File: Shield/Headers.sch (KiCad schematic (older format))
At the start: 18 parts, among them J1 EXPANSION, J12 CONN_6, J23 POWER IN, J24 GND V_IN, J28 Probe, J8 Y MOT/STOP, J9 X MOT/STOP

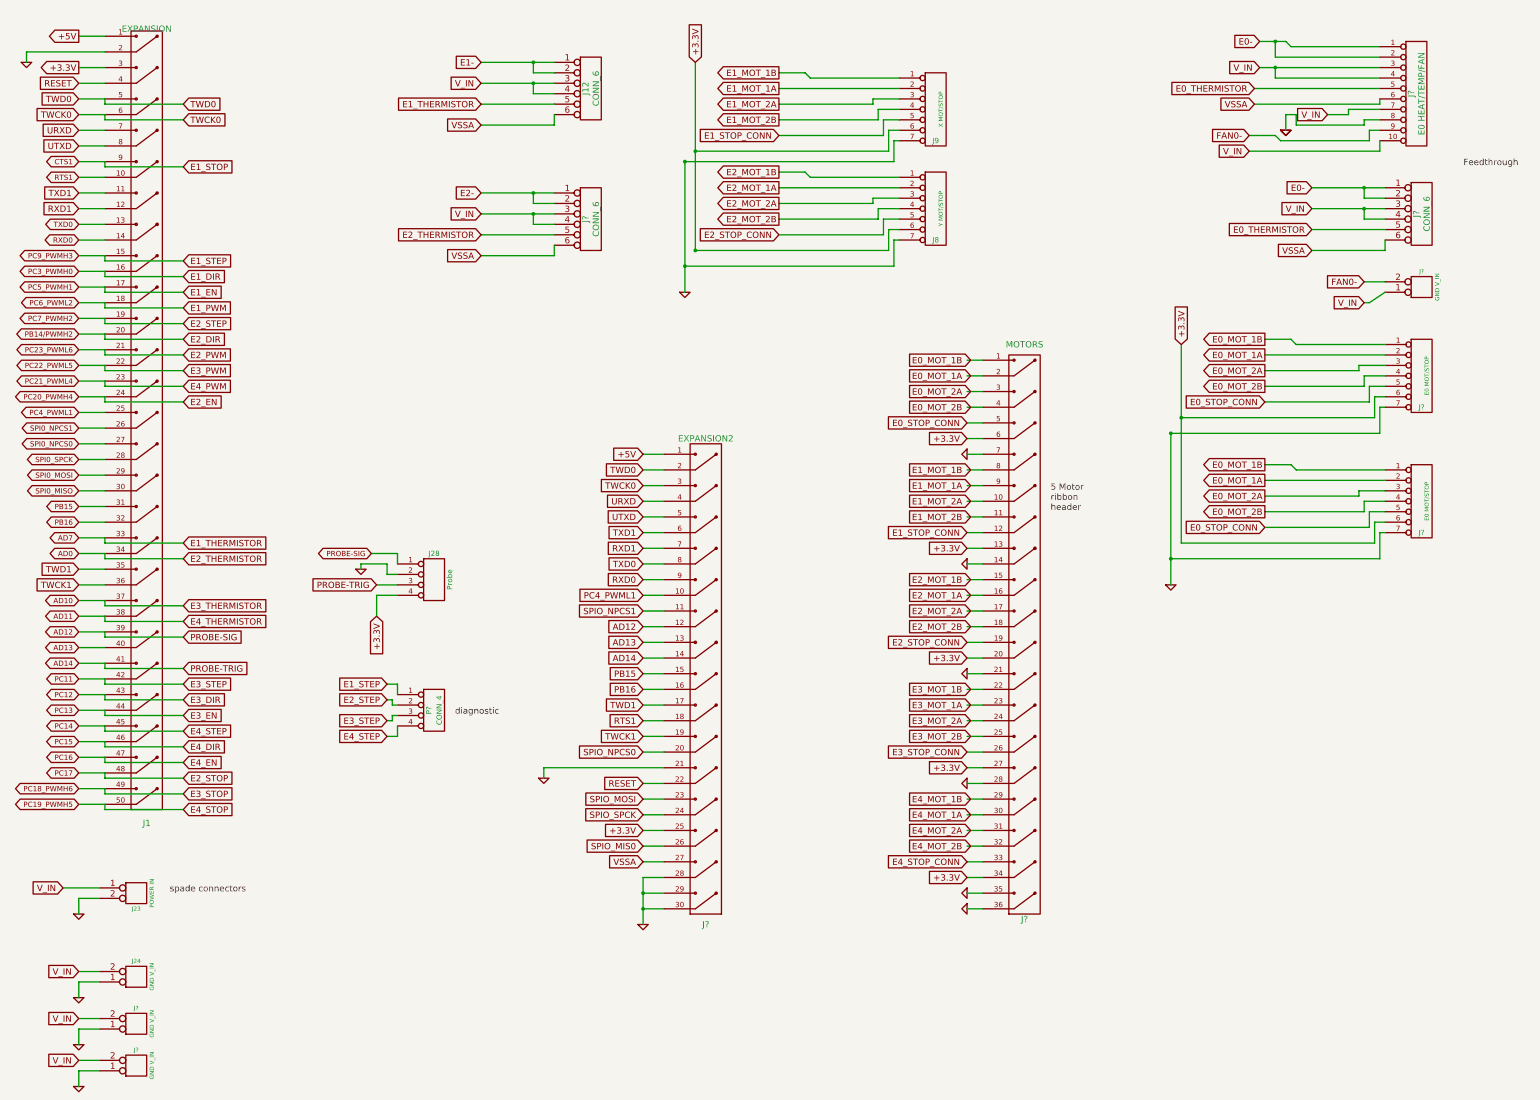
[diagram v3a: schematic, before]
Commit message: Inputs and outputs tidied to keep DRC a bit happier...
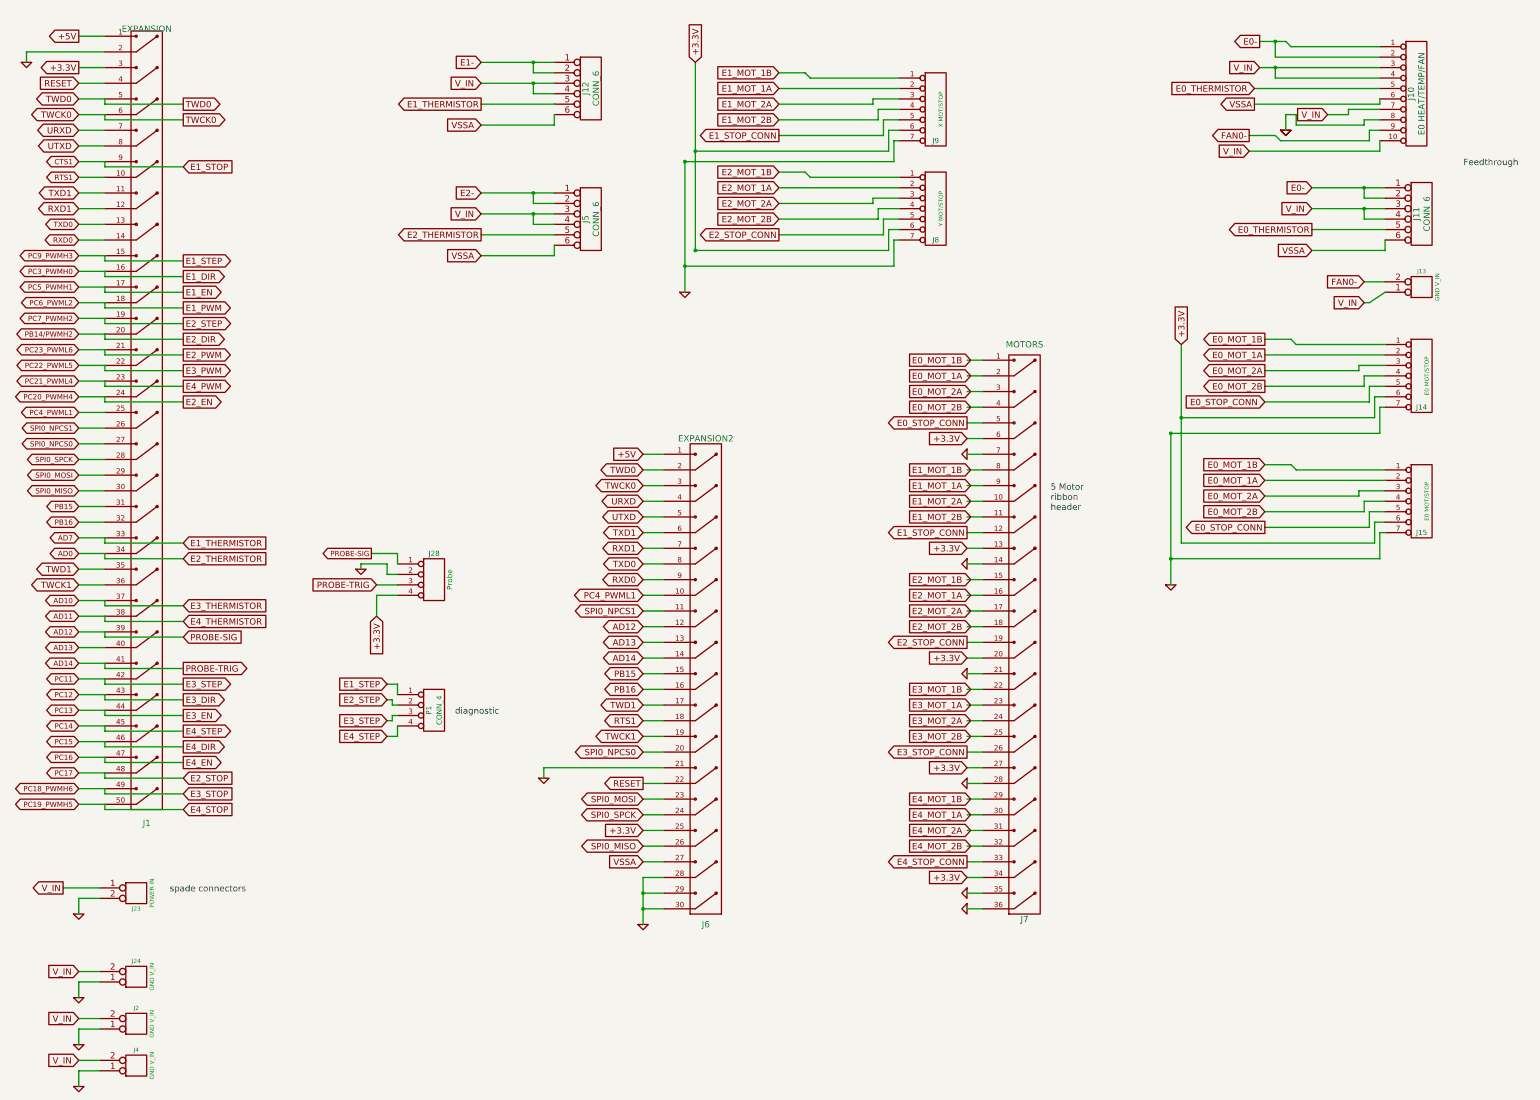
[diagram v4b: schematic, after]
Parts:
- gave numbers to parts that had none: 11
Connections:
- net labels removed: SPIO_MIS0, SPIO_MOSI, SPIO_NPCS0, SPIO_NPCS1, SPIO_SPCK
- wire segments 357 -> 343

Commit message: Header labels corrected.
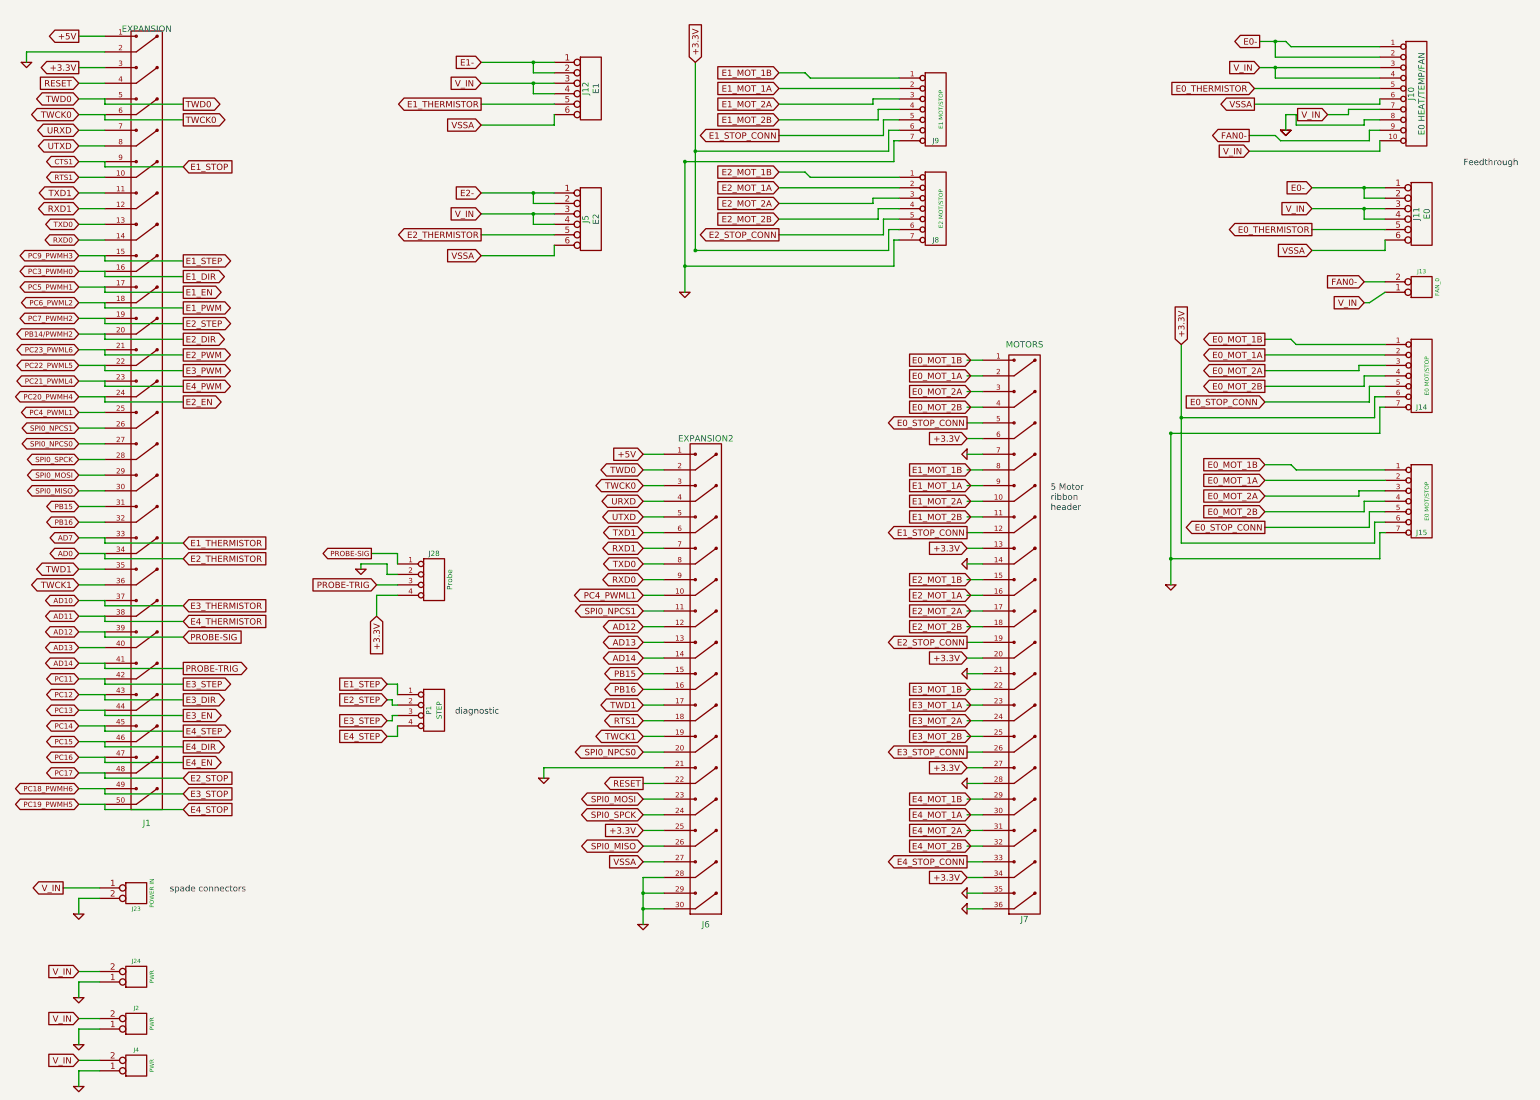
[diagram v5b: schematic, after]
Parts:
- J11: value CONN_6 -> E0
- J12: value CONN_6 -> E1
- J13: value GND V_IN -> FAN_0
- J2, J24, J4: value GND V_IN -> PWR
- J5: value CONN_6 -> E2
- J8: value Y MOT/STOP -> E2 MOT/STOP
- J9: value X MOT/STOP -> E1 MOT/STOP
- P1: value CONN_4 -> STEP
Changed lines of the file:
@@
-EESchema Schematic File Version 2  date Fri 07 Nov 2014 11:38:16 GMT
+EESchema Schematic File Version 2  date Fri 07 Nov 2014 14:33:05 GMT
 LIBS:power
 LIBS:device
@@
 P 5000 7150
 F 0 "P1" V 4950 7150 50  0000 C CNN
-F 1 "CONN_4" V 5050 7150 50  0000 C CNN
+F 1 "STEP" V 5050 7150 50  0000 C CNN
 	1    5000 7150
 	1    0    0    -1
@@
 P 14450 3050
 F 0 "J13" H 14450 2950 40  0000 C CNN
-F 1 "GND  V_IN" V 14600 3100 40  0000 C CNN
+F 1 "FAN_0" V 14600 3100 40  0000 C CNN
 	1    14450 3050
 	1    0    0    1
@@
 P 14450 2400
 F 0 "J11" V 14400 2400 60  0000 C CNN
-F 1 "CONN_6" V 14500 2400 60  0000 C CNN
+F 1 "E0" V 14500 2400 60  0000 C CNN
 	1    14450 2400
 	1    0    0    -1
@@
 P 2150 10500
 F 0 "J4" H 2150 10400 40  0000 C CNN
-F 1 "GND  V_IN" V 2300 10550 40  0000 C CNN
+F 1 "PWR" V 2300 10550 40  0000 C CNN
 	1    2150 10500
 	1    0    0    1
@@
 P 2150 10100
 F 0 "J2" H 2150 10000 40  0000 C CNN
-F 1 "GND  V_IN" V 2300 10150 40  0000 C CNN
+F 1 "PWR" V 2300 10150 40  0000 C CNN
 	1    2150 10100
 	1    0    0    1
@@
 P 6500 2450
 F 0 "J5" V 6450 2450 60  0000 C CNN
-F 1 "CONN_6" V 6550 2450 60  0000 C CNN
+F 1 "E2" V 6550 2450 60  0000 C CNN
 	1    6500 2450
 	1    0    0    -1
@@
 P 6500 1200
 F 0 "J12" V 6450 1200 60  0000 C CNN
-F 1 "CONN_6" V 6550 1200 60  0000 C CNN
+F 1 "E1" V 6550 1200 60  0000 C CNN
 	1    6500 1200
 	1    0    0    -1
@@
 P 2150 9650
 F 0 "J24" H 2150 9550 40  0000 C CNN
-F 1 "GND  V_IN" V 2300 9700 40  0000 C CNN
+F 1 "PWR" V 2300 9700 40  0000 C CNN
 	1    2150 9650
 	1    0    0    1
@@
 P 9800 1400
 F 0 "J9" H 9800 1100 50  0000 C CNN
-F 1 "X MOT/STOP" V 9850 1400 40  0000 C CNN
+F 1 "E1 MOT/STOP" V 9850 1400 40  0000 C CNN
 	1    9800 1400
 	1    0    0    -1
@@
 P 9800 2350
 F 0 "J8" H 9800 2050 50  0000 C CNN
-F 1 "Y MOT/STOP" V 9850 2350 40  0000 C CNN
+F 1 "E2 MOT/STOP" V 9850 2350 40  0000 C CNN
 	1    9800 2350
 	1    0    0    -1

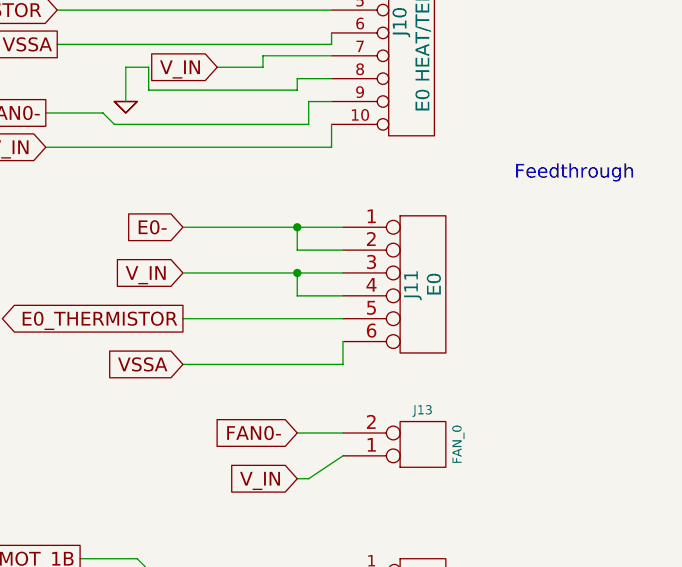
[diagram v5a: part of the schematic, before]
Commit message: Started PCB layout for Shield.
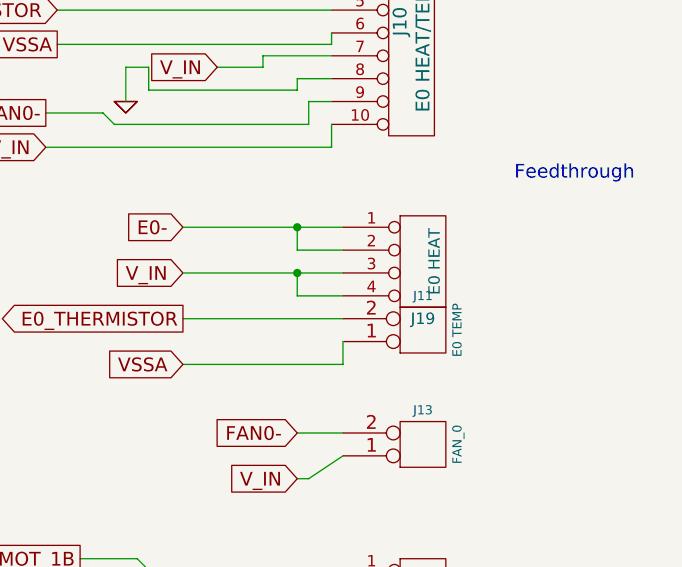
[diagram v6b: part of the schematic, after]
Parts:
- removed J11: E0, symbol CONN_6
- added J11: E0 TEMP, symbol CONN2
- added J19: E0 HEAT, symbol CONN4
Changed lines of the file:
@@
-EESchema Schematic File Version 2  date Fri 07 Nov 2014 14:33:05 GMT
+EESchema Schematic File Version 2  date Thu 13 Nov 2014 23:27:25 GMT
 LIBS:power
 LIBS:device
@@
 Sheet 3 4
 Title "Duet"
-Date "7 nov 2014"
+Date "13 nov 2014"
 Rev "0.7"
 Comp "Think3DPrint3D, RepRapPro"
@@
 Comment4 ""
 $EndDescr
+$Comp
+L CONN4 J19
+U 1 1 5465390C
+P 14450 2300
+F 0 "J19" H 14450 2050 50  0000 C CNN
+F 1 "E0 HEAT" V 14500 2300 50  0000 C CNN
+	1    14450 2300
+	1    0    0    -1
+$EndComp
+$Comp
+L CONN2 J11
+U 1 1 5464EB0A
+P 14450 2550
+F 0 "J11" H 14450 2450 40  0000 C CNN
+F 1 "E0 TEMP" V 14600 2600 40  0000 C CNN
+	1    14450 2550
+	1    0    0    1
+$EndComp
 Text GLabel 7000 6650 0    60   BiDi ~ 0
 AD14
@@
 Text GLabel 13900 3050 0    60   Input ~ 0
 FAN0-
-$Comp
-L CONN_6 J11
-U 1 1 545B8869
-P 14450 2400
-F 0 "J11" V 14400 2400 60  0000 C CNN
-F 1 "E0" V 14500 2400 60  0000 C CNN
-	1    14450 2400
-	1    0    0    -1
-$EndComp
 Text GLabel 13400 2150 0    60   Input ~ 0
 E0-

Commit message: Minor tidying...
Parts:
- removed J10: E0 HEAT/TEMP/FAN, symbol CONN_10
- added J10: CONN2, symbol CONN2
- added K1: CONN_3, symbol CONN_3
- added P2: CONN_6, symbol CONN_6
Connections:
- wire segments 343 -> 347

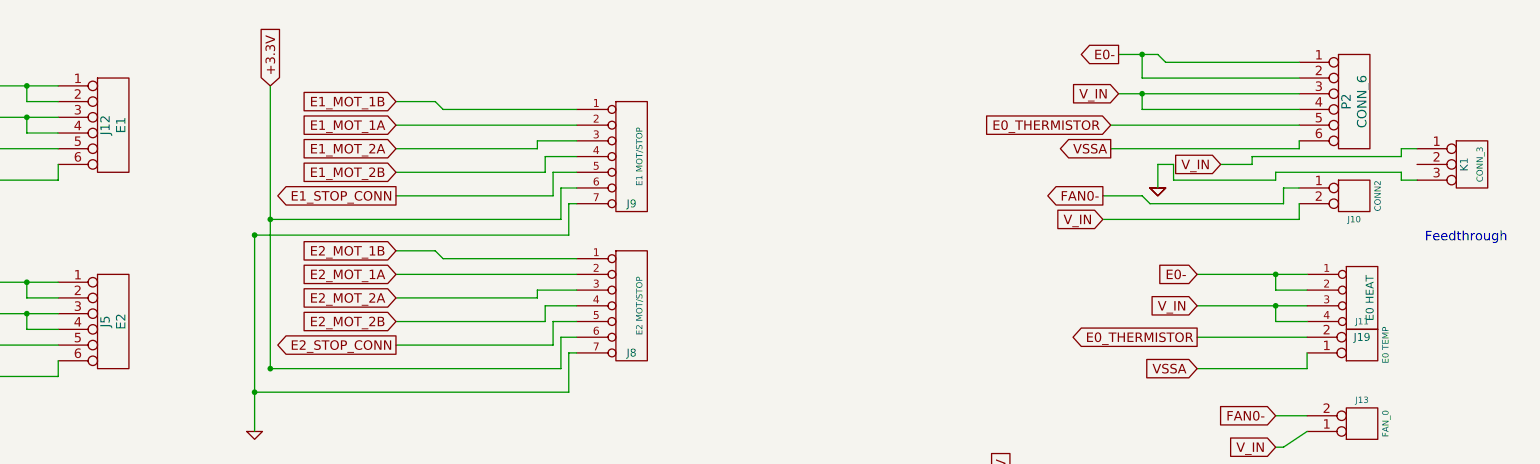
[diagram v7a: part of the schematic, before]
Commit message: Some pin headers provisionally positioned.
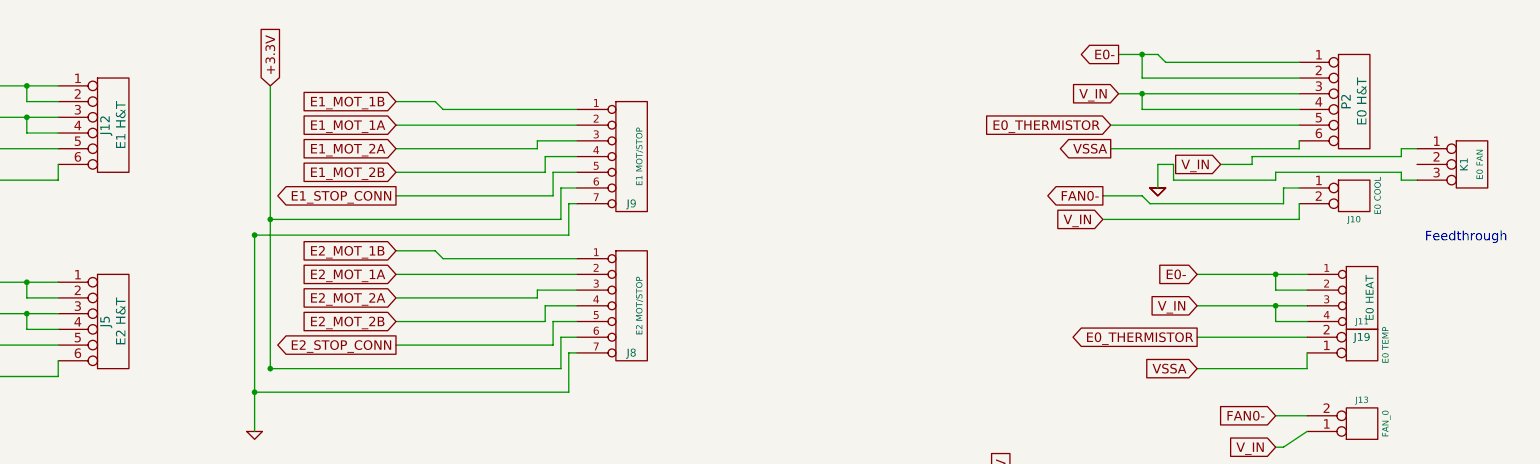
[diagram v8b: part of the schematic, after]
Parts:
- J10: value CONN2 -> E0 COOL
- J12: value E1 -> E1 H&T
- J5: value E2 -> E2 H&T
- K1: value CONN_3 -> E0 FAN
- P2: value CONN_6 -> E0 H&T
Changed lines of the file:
@@
-EESchema Schematic File Version 2  date Fri 14 Nov 2014 12:57:57 GMT
+EESchema Schematic File Version 2  date Fri 14 Nov 2014 15:03:09 GMT
 LIBS:power
 LIBS:device
@@
 P 15150 1450
 F 0 "K1" V 15100 1450 50  0000 C CNN
-F 1 "CONN_3" V 15200 1450 40  0000 C CNN
+F 1 "E0 FAN" V 15200 1450 40  0000 C CNN
 	1    15150 1450
 	1    0    0    -1
@@
 P 14400 1700
 F 0 "J10" H 14400 1600 40  0000 C CNN
-F 1 "CONN2" V 14550 1750 40  0000 C CNN
+F 1 "E0 COOL" V 14550 1750 40  0000 C CNN
 	1    14400 1700
 	1    0    0    -1
@@
 P 14400 1050
 F 0 "P2" V 14350 1050 60  0000 C CNN
-F 1 "CONN_6" V 14450 1050 60  0000 C CNN
+F 1 "E0 H&T" V 14450 1050 60  0000 C CNN
 	1    14400 1050
 	1    0    0    -1
@@
 P 6500 2450
 F 0 "J5" V 6450 2450 60  0000 C CNN
-F 1 "E2" V 6550 2450 60  0000 C CNN
+F 1 "E2 H&T" V 6550 2450 60  0000 C CNN
 	1    6500 2450
 	1    0    0    -1
@@
 P 6500 1200
 F 0 "J12" V 6450 1200 60  0000 C CNN
-F 1 "E1" V 6550 1200 60  0000 C CNN
+F 1 "E1 H&T" V 6550 1200 60  0000 C CNN
 	1    6500 1200
 	1    0    0    -1
